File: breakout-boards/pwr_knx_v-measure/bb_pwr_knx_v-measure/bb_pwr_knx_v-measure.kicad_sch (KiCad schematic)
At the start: 50 parts, among them IC1 TPS560430, T1 BC856, T2 FZT753, T3 BC847

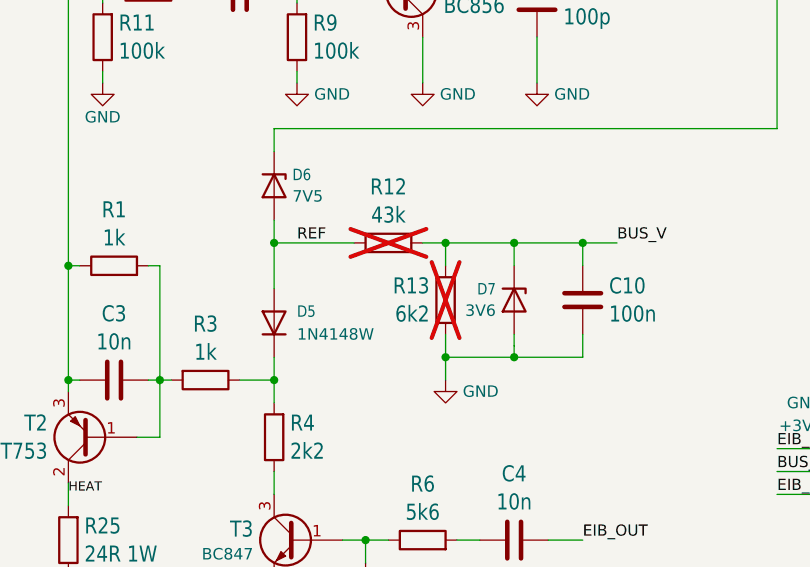
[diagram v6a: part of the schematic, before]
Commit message: controllers: reduce osc load, fix DNP for voltage measurement
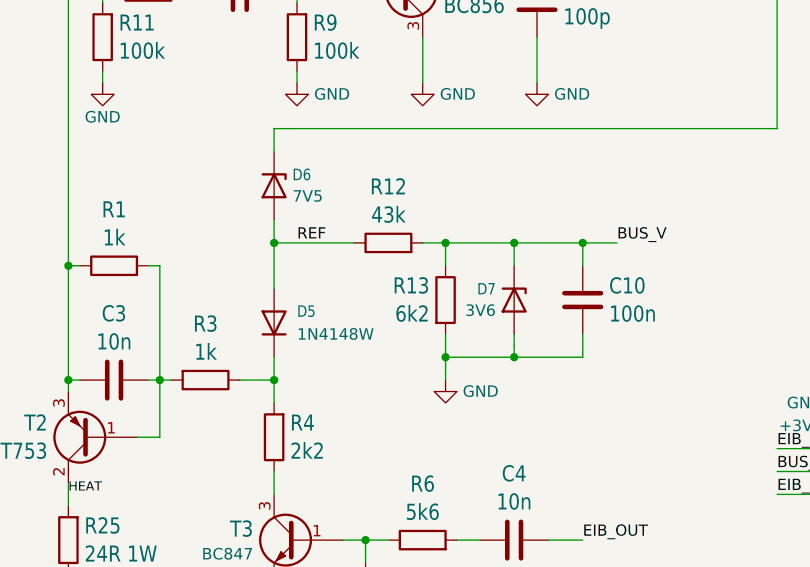
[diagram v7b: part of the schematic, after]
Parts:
- R12, R13: now fitted; now in the parts list
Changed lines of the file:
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@@
 		(unit 1)
 		(exclude_from_sim no)
-		(in_bom no)
-		(on_board yes)
-		(dnp yes)
+		(in_bom yes)
+		(on_board yes)
+		(dnp no)
 		(fields_autoplaced yes)
 		(property "Reference" "R13"
@@
 		(unit 1)
 		(exclude_from_sim no)
-		(in_bom no)
-		(on_board yes)
-		(dnp yes)
+		(in_bom yes)
+		(on_board yes)
+		(dnp no)
 		(fields_autoplaced yes)
 		(property "Reference" "R12"
